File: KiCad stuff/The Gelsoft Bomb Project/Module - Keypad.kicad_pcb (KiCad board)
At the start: 2 copper layers, 52.1 x 44.5 mm, 7 parts, among them J1 ISP, J2 Module Connector, U1 ATmega8-16PU, U2 74HC595, U3 3x4_Keypad, U4 SUR1601B

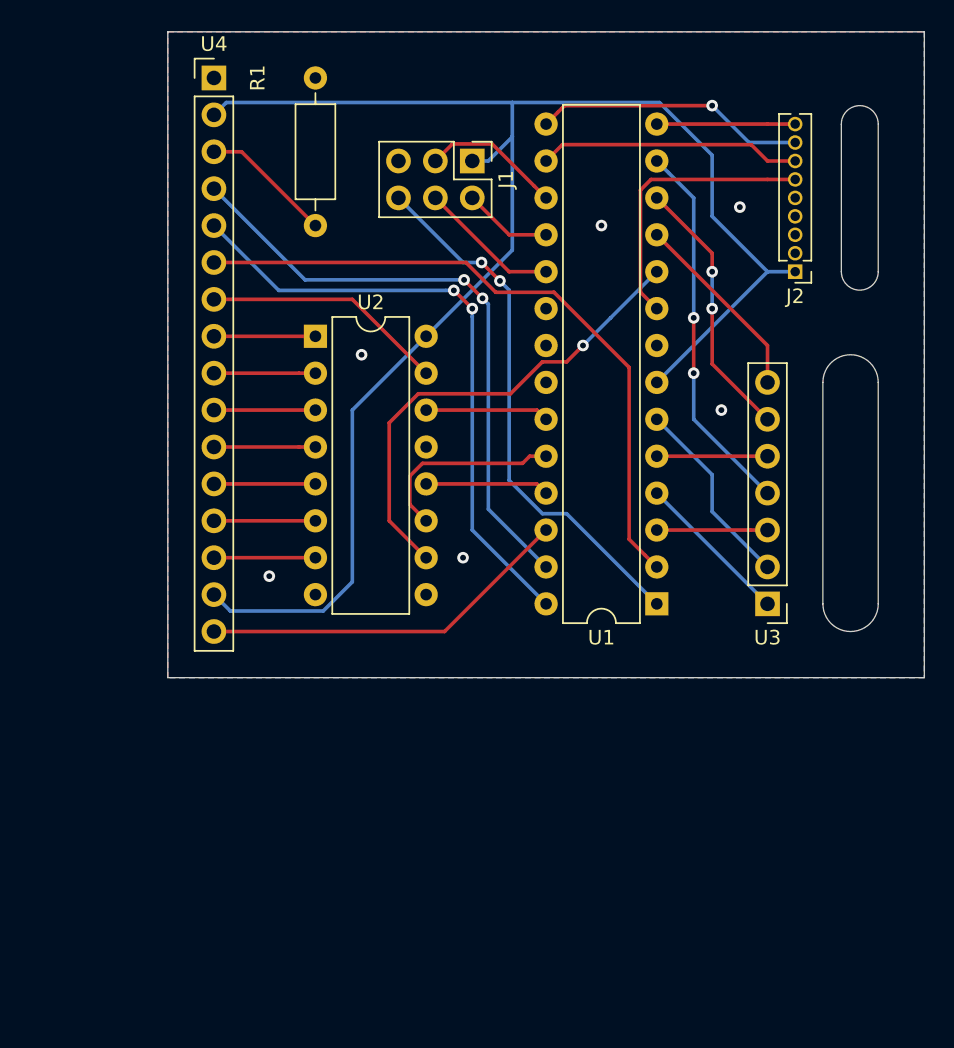
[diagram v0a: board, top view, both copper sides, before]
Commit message: Revise PCB for new pinout
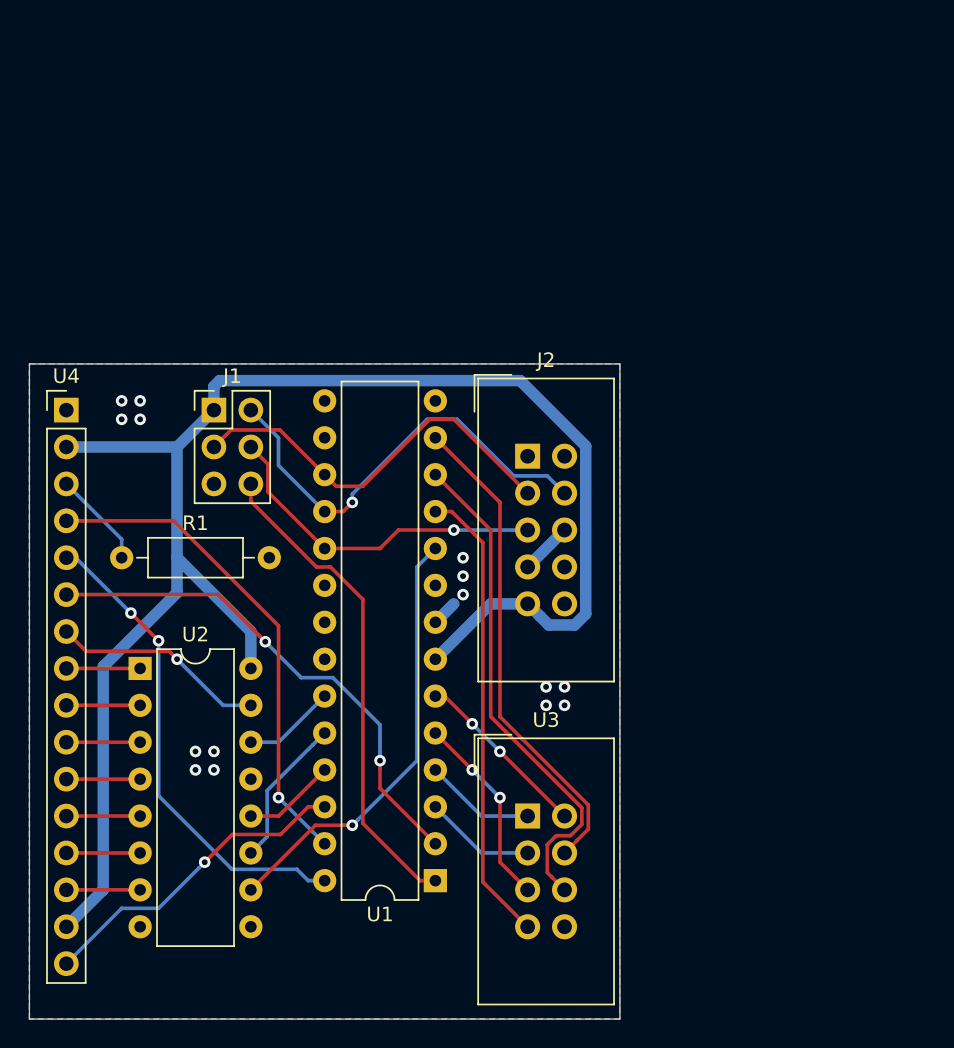
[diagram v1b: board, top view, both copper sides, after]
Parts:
- J2: footprint Connector_PinHeader_1.27mm:PinHeader_1x09_P1.27mm_Vertical -> Connector_IDC:IDC-Header_2x05_P2.54mm_Vertical
- U3: footprint Connector_PinHeader_2.54mm:PinHeader_1x07_P2.54mm_Vertical -> Connector_IDC:IDC-Header_2x04_P2.54mm_Vertical
- U4: value SUR1601B -> MC11605A6W7-BNMLW
- moved R1 26.5 mm to (97.2, 122.6), turned to 0 degrees
- moved U2 25.8 mm to (98.4, 130.2)
- moved U4 25.0 mm to (93.3, 112.4)
- moved J1 24.7 mm to (103.5, 112.4), turned to 0 degrees
- moved U1 24.4 mm to (118.7, 144.8)
- moved J2 22.4 mm to (125.1, 115.6), turned to 0 degrees
- moved U3 22.0 mm to (125.1, 140.3), turned to 0 degrees
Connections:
- J2 pad 1: 5v -> Earth
- J2 pad 2: VIN -> Earth
- J2 pad 3: Net-(J2-Pad3) -> MOSI
- J2 pad 4: Net-(J2-Pad4) -> MISO
- J2 pad 5: Earth -> SCK
- J2 pad 6: LOWPOWER -> Earth
- J2 pad 7: DISARM -> Earth
- J2 pad 8: STRIKE -> VIN
- J2 pad 9: CORRECT -> 5v
- U1 pad 14: CORRECT -> Net-(U1-Pad14)
- U1 pad 15: STRIKE -> Net-(U1-Pad15)
- U1 pad 16: DISARM -> Net-(U1-Pad16)
- U1 pad 9: LOWPOWER -> Net-(U1-Pad9)
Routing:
- net MISO: track 6.13 -> 30.7 mm, vias 0 -> 1
- net LOWPOWER: track 19.6 -> 0.00 mm
- net STRIKE: track 18.7 -> 0.00 mm, vias 1 -> 0
- net Net-(U1-Pad11): track 13.3 -> 31.9 mm
- net DISARM: track 18.1 -> 0.00 mm
- net MOSI: track 9.65 -> 27.7 mm
- net Net-(U1-Pad12): track 18.4 -> 34.8 mm, vias 2 -> 0
- net SCK: track 9.72 -> 23.6 mm, vias 0 -> 1
- net Net-(U1-Pad2): track 46.1 -> 35.1 mm, vias 0 -> 2
- net CORRECT: track 9.52 -> 0.00 mm
- net Net-(U1-Pad28): track 42.6 -> 33.2 mm
- net Net-(U1-Pad27): track 42.1 -> 33.9 mm, vias 2 -> 1
- net Net-(U1-Pad13): track 26.0 -> 33.6 mm, vias 2 -> 0
- net Net-(U1-Pad5): track 7.62 -> 13.4 mm, vias 0 -> 2
- net Earth: track 0.00 -> 5.39 mm, vias 6 -> 15
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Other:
- board size 52.1 x 44.5 mm -> 40.6 x 45.1 mm
